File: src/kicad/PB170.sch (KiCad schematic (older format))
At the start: 51 parts, among them J2 USB_B_Micro, Q1 BC817, Q2 BC817, Q3 BC817, Q4 BC817, SW1 SW_MEC_5E, U1 74HC08, U20 74LS73, U21 74LS73

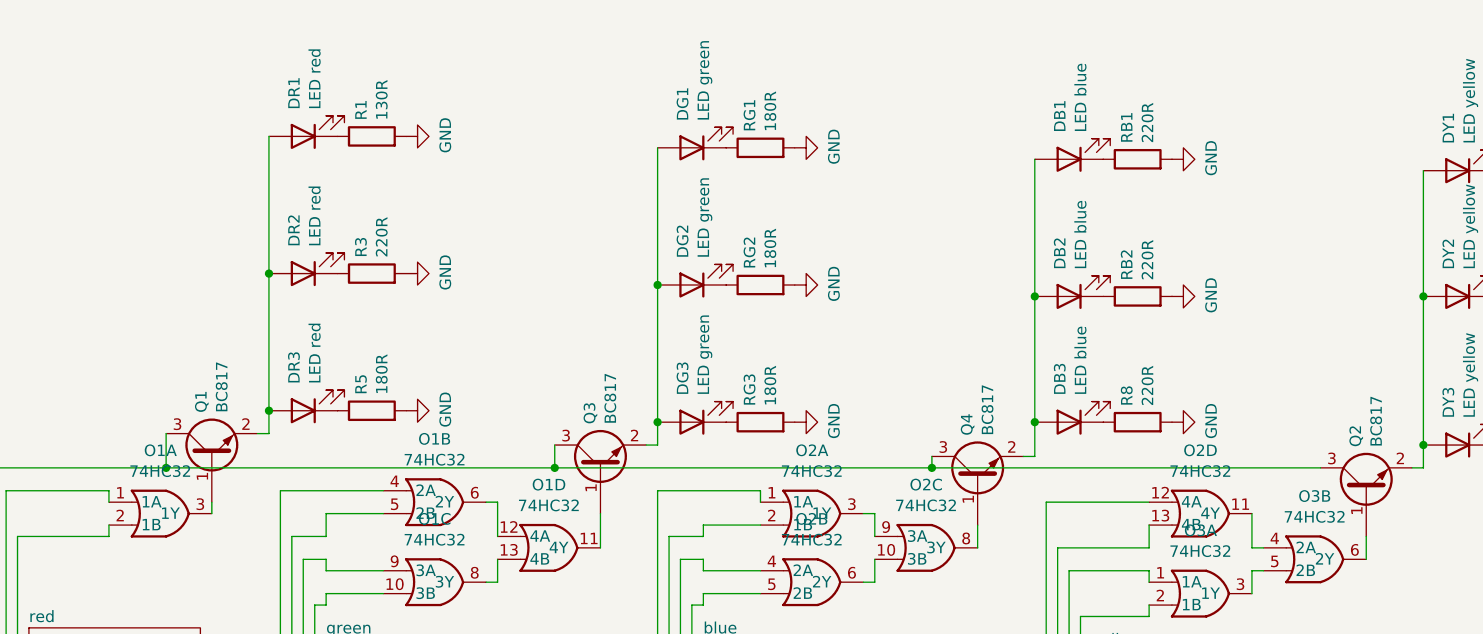
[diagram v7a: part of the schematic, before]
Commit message: Fixed wires under parts - removed
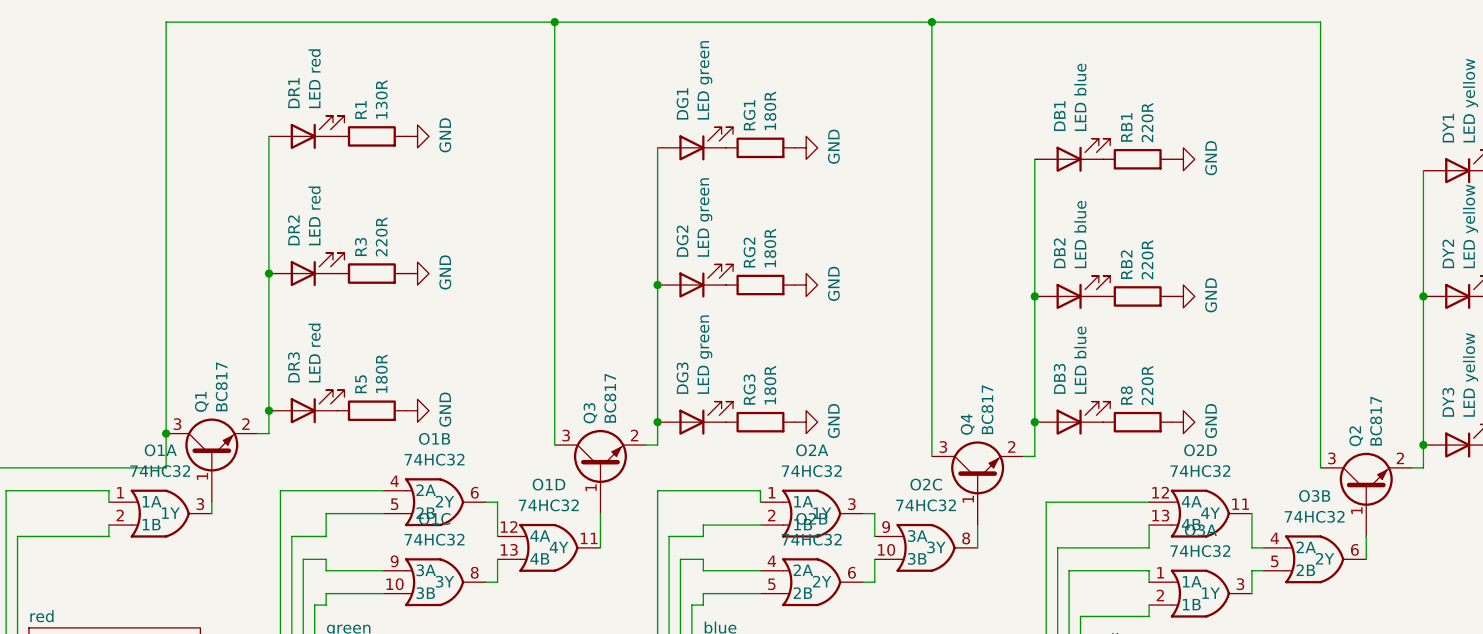
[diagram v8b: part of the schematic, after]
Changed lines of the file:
@@
 Wire Wire Line
 	4750 2450 4750 2300
-Wire Wire Line
-	4750 2450 6450 2450
-Connection ~ 6450 2450
-Wire Wire Line
-	6450 2450 8100 2450
-Wire Wire Line
-	8100 2450 8100 2400
-Connection ~ 8100 2450
-Wire Wire Line
-	8100 2450 9800 2450
-Connection ~ 4750 2450
 Connection ~ 2650 6350
 Text Notes 3350 6900 0    50   ~ 0
@@
 Wire Wire Line
 	2650 6900 4250 6900
-Wire Wire Line
-	6450 2350 6450 2450
 $Comp
 L Transistor_BJT:BC817 Q?
@@
 Text GLabel 9600 6300 0    50   Input ~ 0
 555output
+Wire Wire Line
+	4750 2300 4750 500
+Wire Wire Line
+	4750 500  6450 500
+Wire Wire Line
+	9800 500  9800 2450
+Connection ~ 4750 2300
+Wire Wire Line
+	6450 2350 6450 500
+Connection ~ 6450 500
+Wire Wire Line
+	6450 500  8100 500
+Wire Wire Line
+	8100 2400 8100 500
+Connection ~ 8100 500
+Wire Wire Line
+	8100 500  9800 500
 $EndSCHEMATC
